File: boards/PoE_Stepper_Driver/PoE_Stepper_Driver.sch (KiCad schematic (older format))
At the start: 13 parts

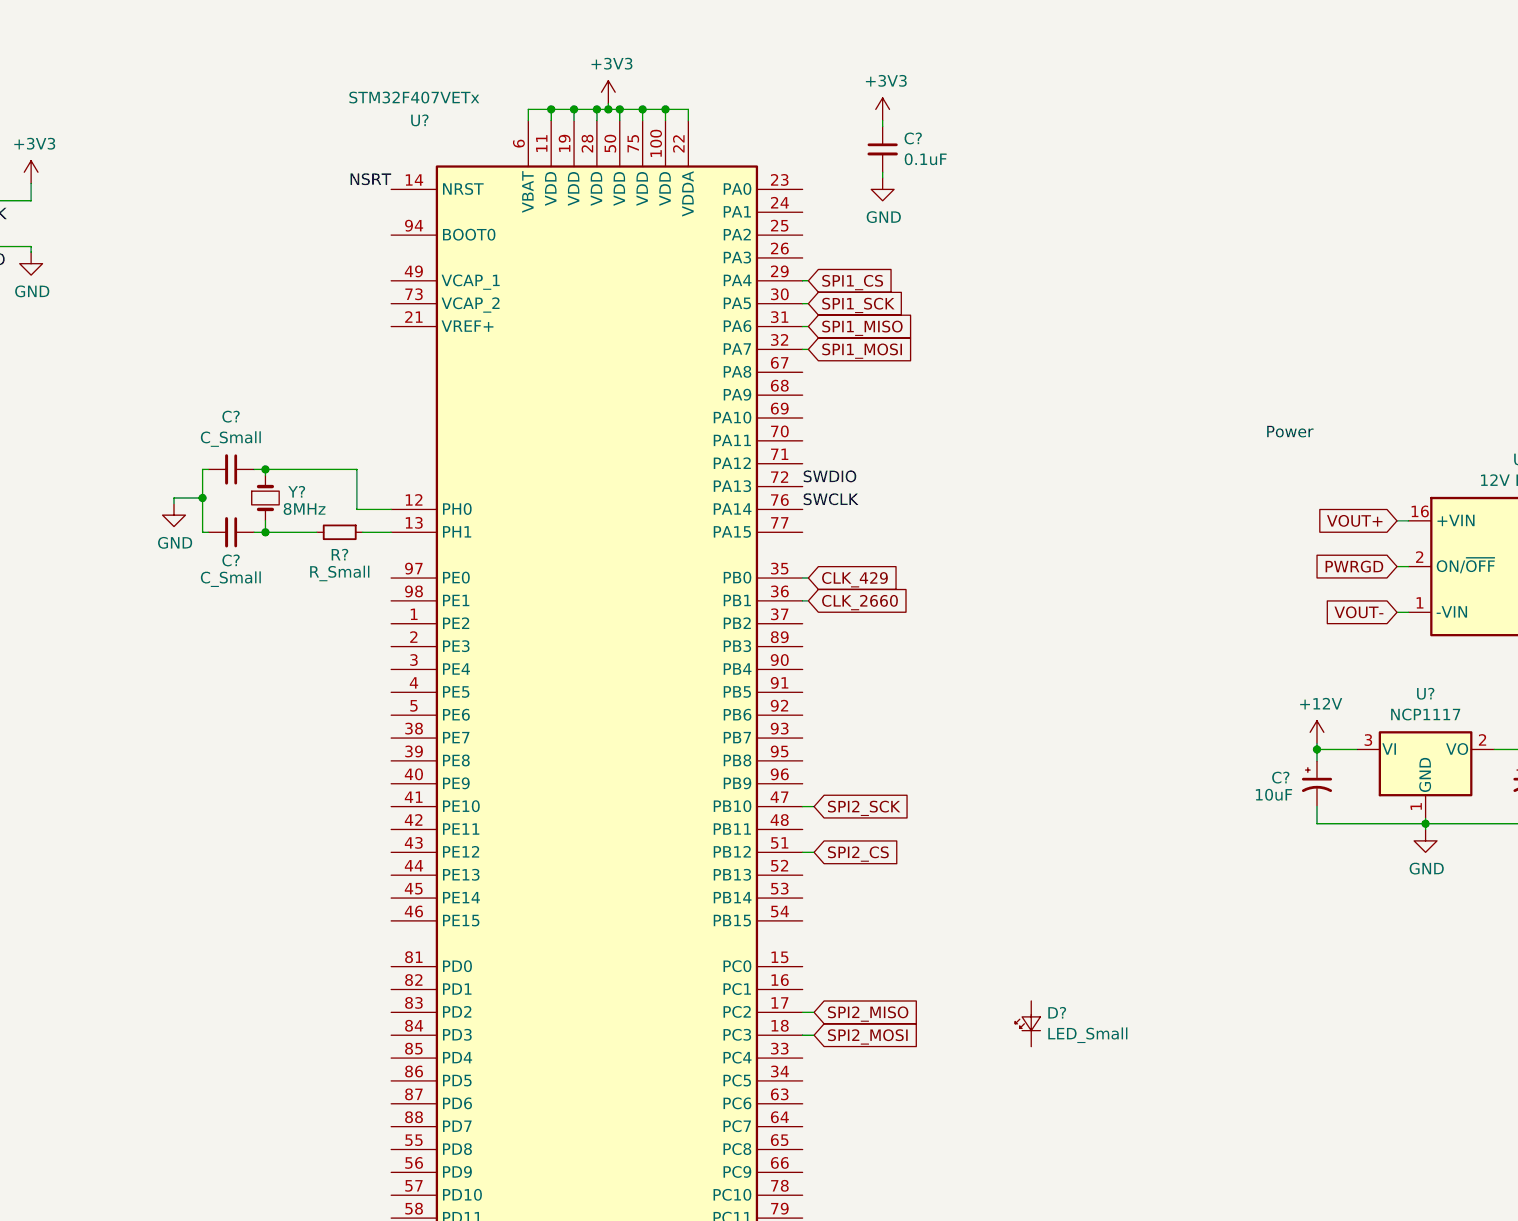
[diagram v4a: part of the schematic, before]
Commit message: added phy schematic symbol
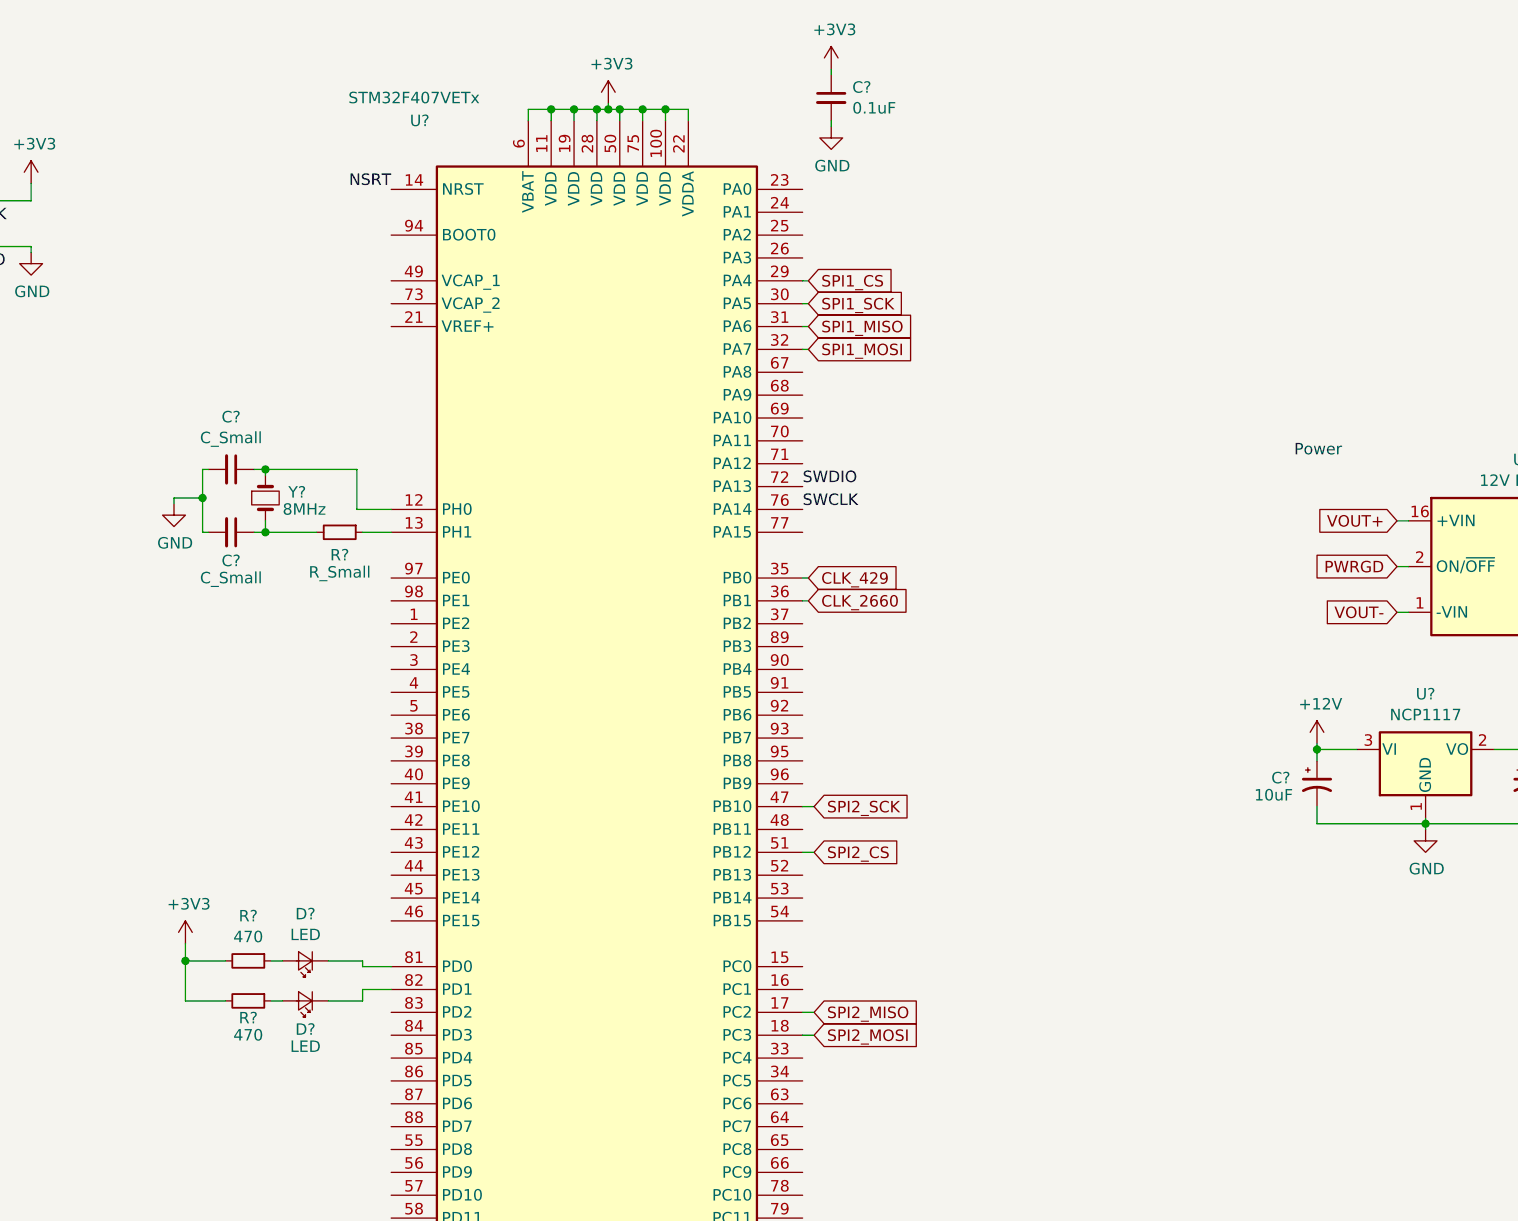
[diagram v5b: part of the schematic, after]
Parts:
- removed D?: LED_Small, symbol device:LED_Small
- added D? (x2): LED, symbol device:LED_Small
- added R? (x2): 470, symbol device:R_Small
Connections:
- net +3V3: now also R?.2, R?.2
- net at U?.81 (PD0): now also D?.1 (K)
- net at U?.82 (PD1): now also D?.1 (K)
- new net: D?.2 (A), R?.1 (x2)
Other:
- moved on the sheet: C?
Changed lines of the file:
@@
 	1    0    0    -1
 $EndComp
-Text Notes 8650 2375 0    50   ~ 0
+Text Notes 8775 2450 0    50   ~ 0
 Power
 $Comp
 L device:C_Small C?
 U 1 1 62172784
-P 6975 1100
-F 0 "C?" H 7067 1146 50  0000 L CNN
-F 1 "0.1uF" H 7067 1055 50  0000 L CNN
-F 2 "" H 6975 1100 50  0001 C CNN
-F 3 "~" H 6975 1100 50  0001 C CNN
-	1    6975 1100
+P 6750 875
+F 0 "C?" H 6842 921 50  0000 L CNN
+F 1 "0.1uF" H 6842 830 50  0000 L CNN
+F 2 "" H 6750 875 50  0001 C CNN
+F 3 "~" H 6750 875 50  0001 C CNN
+	1    6750 875
 	1    0    0    -1
 $EndComp
@@
 L power:GND #PWR?
 U 1 1 62173490
-P 6975 1225
-F 0 "#PWR?" H 6975 975 50  0001 C CNN
-F 1 "GND" H 6980 1052 50  0000 C CNN
-F 2 "" H 6975 1225 50  0001 C CNN
-F 3 "" H 6975 1225 50  0001 C CNN
-	1    6975 1225
-	1    0    0    -1
-$EndComp
-Wire Wire Line
-	6975 1200 6975 1225
+P 6750 1000
+F 0 "#PWR?" H 6750 750 50  0001 C CNN
+F 1 "GND" H 6755 827 50  0000 C CNN
+F 2 "" H 6750 1000 50  0001 C CNN
+F 3 "" H 6750 1000 50  0001 C CNN
+	1    6750 1000
+	1    0    0    -1
+$EndComp
+Wire Wire Line
+	6750 975  6750 1000
 $Comp
 L power:+3V3 #PWR?
 U 1 1 62174C94
-P 6975 975
-F 0 "#PWR?" H 6975 825 50  0001 C CNN
-F 1 "+3V3" H 6990 1148 50  0000 C CNN
-F 2 "" H 6975 975 50  0001 C CNN
-F 3 "" H 6975 975 50  0001 C CNN
-	1    6975 975
-	1    0    0    -1
-$EndComp
-Wire Wire Line
-	6975 975  6975 1000
+P 6750 750
+F 0 "#PWR?" H 6750 600 50  0001 C CNN
+F 1 "+3V3" H 6765 923 50  0000 C CNN
+F 2 "" H 6750 750 50  0001 C CNN
+F 3 "" H 6750 750 50  0001 C CNN
+	1    6750 750
+	1    0    0    -1
+$EndComp
+Wire Wire Line
+	6750 750  6750 775
 $Comp
 L power:+12V #PWR?
@@
 Text Label 4825 1275 2    50   ~ 0
 NSRT
-$Comp
-L device:LED_Small D?
-U 1 1 623153A1
-P 7625 4925
-F 0 "D?" V 7671 4857 50  0000 R CNN
-F 1 "LED_Small" V 7580 4857 50  0000 R CNN
-F 2 "" V 7625 4925 50  0001 C CNN
-F 3 "~" V 7625 4925 50  0001 C CNN
-	1    7625 4925
-	0    -1   -1   0
-$EndComp
 Text Label 6625 2675 0    50   ~ 0
 SWCLK
@@
 Wire Wire Line
 	6625 4175 6675 4175
+Wire Wire Line
+	4700 4675 4825 4675
+$Comp
+L power:+3V3 #PWR?
+U 1 1 6265F676
+P 3925 4575
+F 0 "#PWR?" H 3925 4425 50  0001 C CNN
+F 1 "+3V3" H 3940 4748 50  0000 C CNN
+F 2 "" H 3925 4575 50  0001 C CNN
+F 3 "" H 3925 4575 50  0001 C CNN
+	1    3925 4575
+	1    0    0    -1
+$EndComp
+$Comp
+L device:R_Small R?
+U 1 1 6266D089
+P 4200 4650
+F 0 "R?" V 4004 4650 50  0000 C CNN
+F 1 "470" V 4095 4650 50  0000 C CNN
+F 2 "" H 4200 4650 50  0001 C CNN
+F 3 "~" H 4200 4650 50  0001 C CNN
+	1    4200 4650
+	0    1    1    0
+$EndComp
+$Comp
+L device:LED_Small D?
+U 1 1 62671C5F
+P 4450 4650
+F 0 "D?" H 4450 4445 50  0000 C CNN
+F 1 "LED" H 4450 4536 50  0000 C CNN
+F 2 "" V 4450 4650 50  0001 C CNN
+F 3 "~" V 4450 4650 50  0001 C CNN
+	1    4450 4650
+	-1   0    0    1
+$EndComp
+Wire Wire Line
+	4300 4650 4350 4650
+$Comp
+L device:R_Small R?
+U 1 1 62679D47
+P 4200 4825
+F 0 "R?" V 4275 4825 50  0000 C CNN
+F 1 "470" V 4350 4825 50  0000 C CNN
+F 2 "" H 4200 4825 50  0001 C CNN
+F 3 "~" H 4200 4825 50  0001 C CNN
+	1    4200 4825
+	0    1    1    0
+$EndComp
+$Comp
+L device:LED_Small D?
+U 1 1 62679D4D
+P 4450 4825
+F 0 "D?" H 4450 4950 50  0000 C CNN
+F 1 "LED" H 4450 5025 50  0000 C CNN
+F 2 "" V 4450 4825 50  0001 C CNN
+F 3 "~" V 4450 4825 50  0001 C CNN
+	1    4450 4825
+	-1   0    0    1
+$EndComp
+Wire Wire Line
+	4300 4825 4350 4825
+Wire Wire Line
+	4550 4650 4700 4650
+Wire Wire Line
+	4700 4650 4700 4675
+Wire Wire Line
+	4550 4825 4700 4825
+Wire Wire Line
+	4700 4825 4700 4775
+Wire Wire Line
+	4700 4775 4825 4775
+Wire Wire Line
+	3925 4575 3925 4650
+Wire Wire Line
+	3925 4825 4100 4825
+Wire Wire Line
+	4100 4650 3925 4650
+Connection ~ 3925 4650
+Wire Wire Line
+	3925 4650 3925 4825
 $EndSCHEMATC

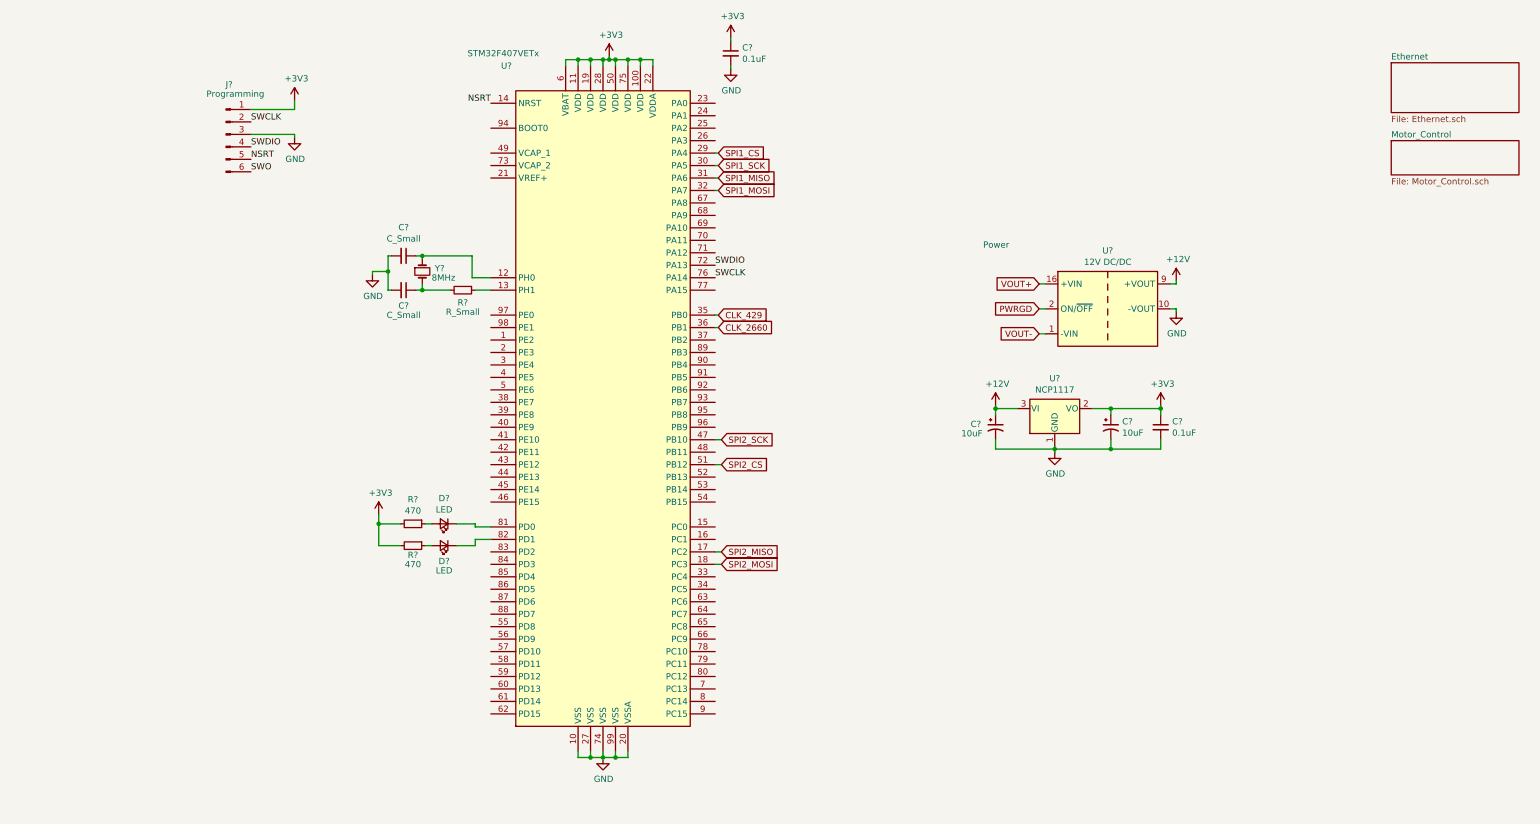
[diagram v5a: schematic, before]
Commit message: added actual phy
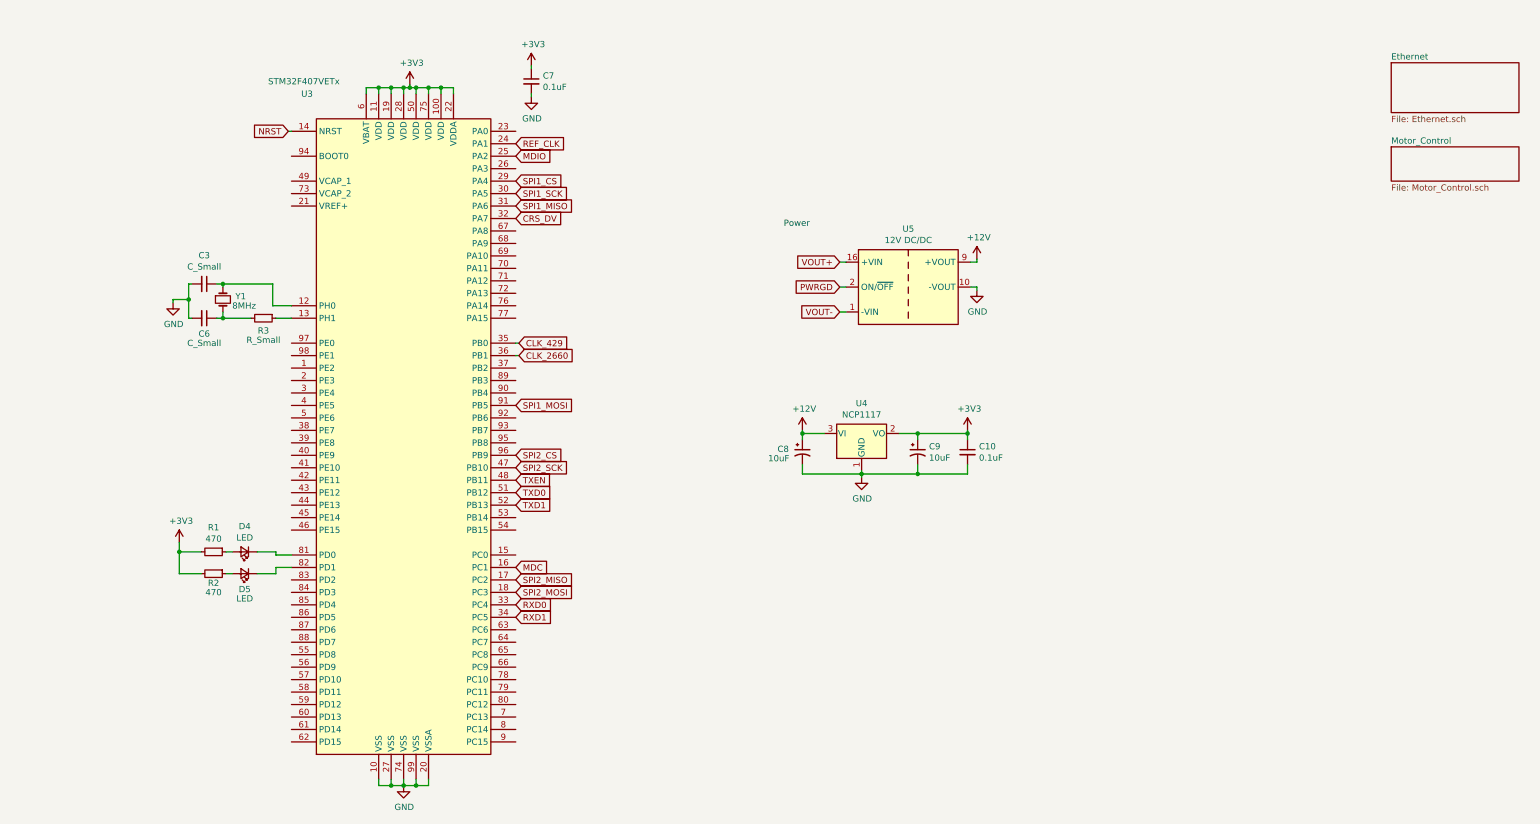
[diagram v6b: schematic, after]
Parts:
- removed J?: Programming, symbol Connector:Conn_01x06_Male
- gave numbers to parts that had none: 15
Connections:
- net SPI1_MOSI: now also U3.91 (PB5); no longer U3.32 (PA7)
- net SPI2_CS: now also U3.96 (PB9); no longer U3.51 (PB12)
- net MDC: now reaches U3.16 (PC1)
- net REF_CLK: now reaches U3.24 (PA1)
- net MDIO: now reaches U3.25 (PA2)
- net RXD0: now reaches U3.33 (PC4)
- net RXD1: now reaches U3.34 (PC5)
- net TXEN: now reaches U3.48 (PB11)
- net TXD1: now reaches U3.52 (PB13)
- net NSRT renamed NRST
- net SWCLK: no longer names the net of U3.76 (PA14)
- net SWDIO: no longer names the net of U3.72 (PA13)
- new net CRS_DV: U3.32 (PA7)
- new net TXD0: U3.51 (PB12)
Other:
- moved on the sheet: C10, C3, C6, C7, C8, C9, D4, D5, R1, R2, R3, U3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
